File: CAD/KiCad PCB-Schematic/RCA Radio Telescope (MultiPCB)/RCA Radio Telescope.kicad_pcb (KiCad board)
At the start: 2 copper layers, 330.1 x 183.4 mm, 67 parts, among them J1 5V In For Filter Board, J10 FILTER_OUT, J11 ANT, J11 Screw_Terminal_01x04, J13 Screw_Terminal_01x04, J15 ANT, J2 9-12V From PoE Splitter, J3 3V Out For LNA, J4 5V Out For Filter Board, J5 Input from SDR, J7 USB_A, J8 USB_A, J9 ANT, Q1 DMP4047LFDE-7, U13 MAX8510EXK30T, U14 TPS62133RGTR, U15 BPF-A1340+, U3 SKY13588-460LF, U4 SKY13588-460LF, U5 SN74AVC2T45DCUR, U6 MIC5365-1.8YC5-TR, U7 MIC5365-3.3YC5-TR

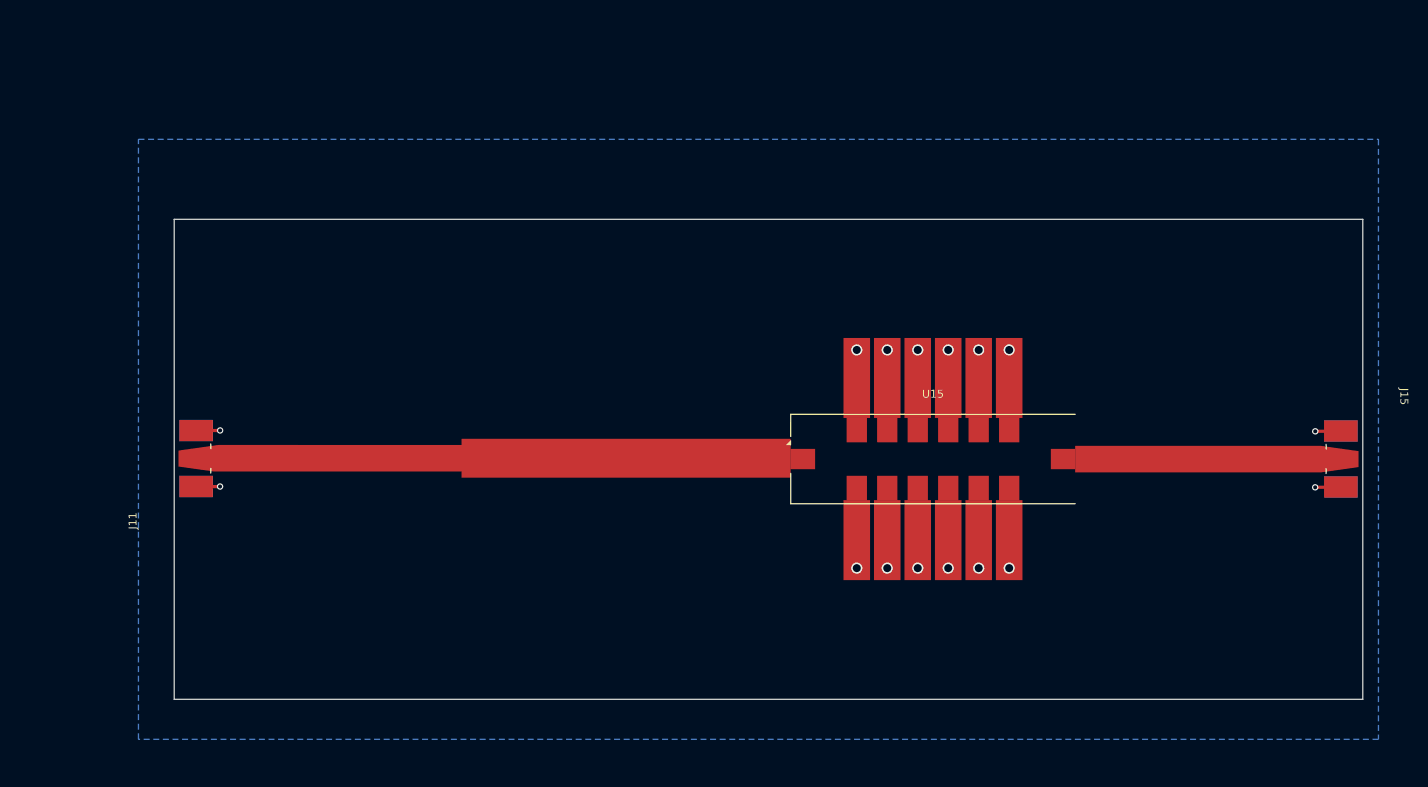
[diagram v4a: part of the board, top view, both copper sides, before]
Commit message: Updated SMD Filter PCB to v1.1
- Adjusted GND pads from 10 to 6mm
- Added M4 Holes for mounting
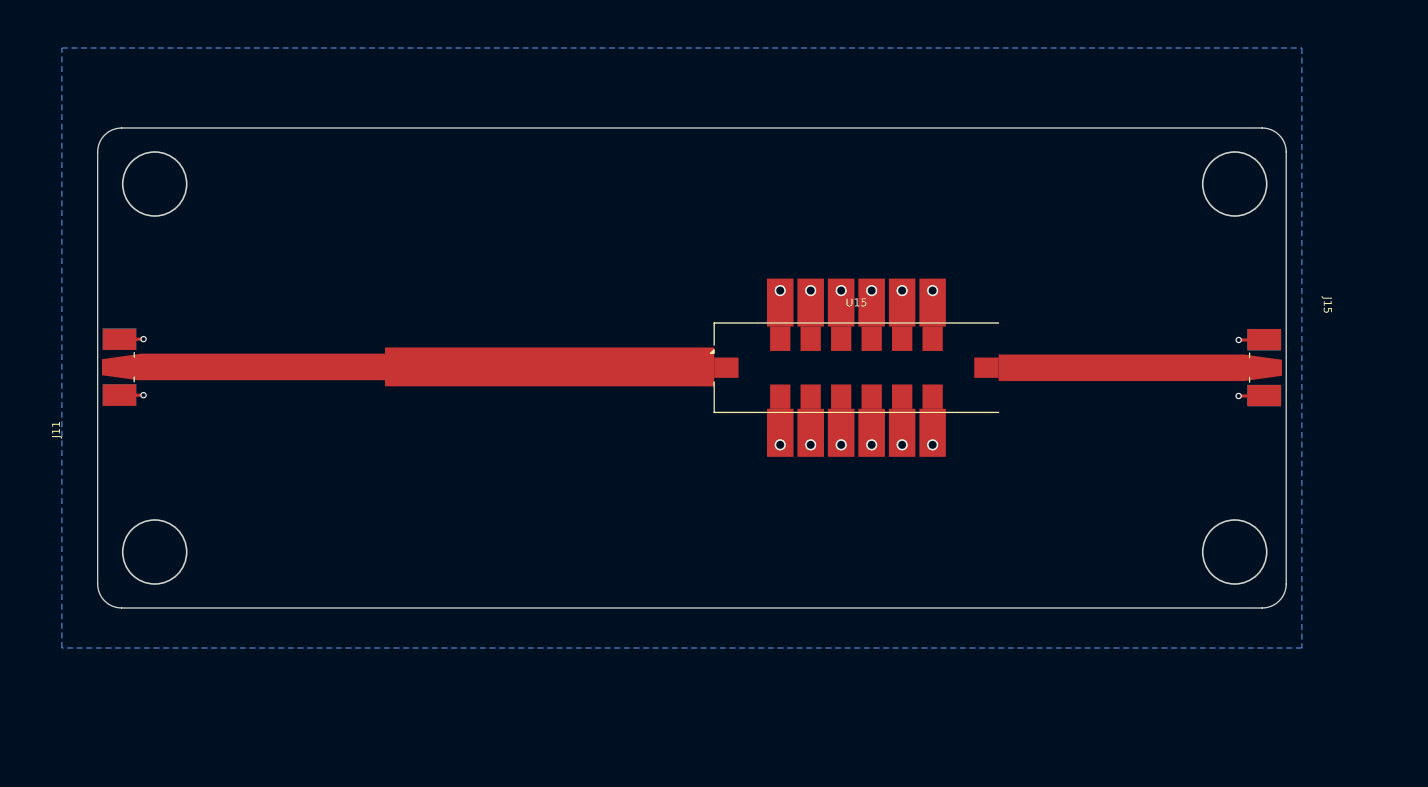
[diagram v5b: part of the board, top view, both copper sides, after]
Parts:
- moved J11 14.9 mm to (197.6, 89.9)
- moved U15 14.9 mm to (294.7, 90.0)
- moved J15 14.9 mm to (350.7, 90.0)
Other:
- board size 330.1 x 183.4 mm -> 320.5 x 183.4 mm
- board text added: "Pad Spacing: 3.81mm"
- board text added: "SMD Filter PCB Rev v1.1 4/9/2025"
- board text removed: "3.81mm"
- board text removed: "SMD Filter PCB Rev v1.0 4/8/2025"

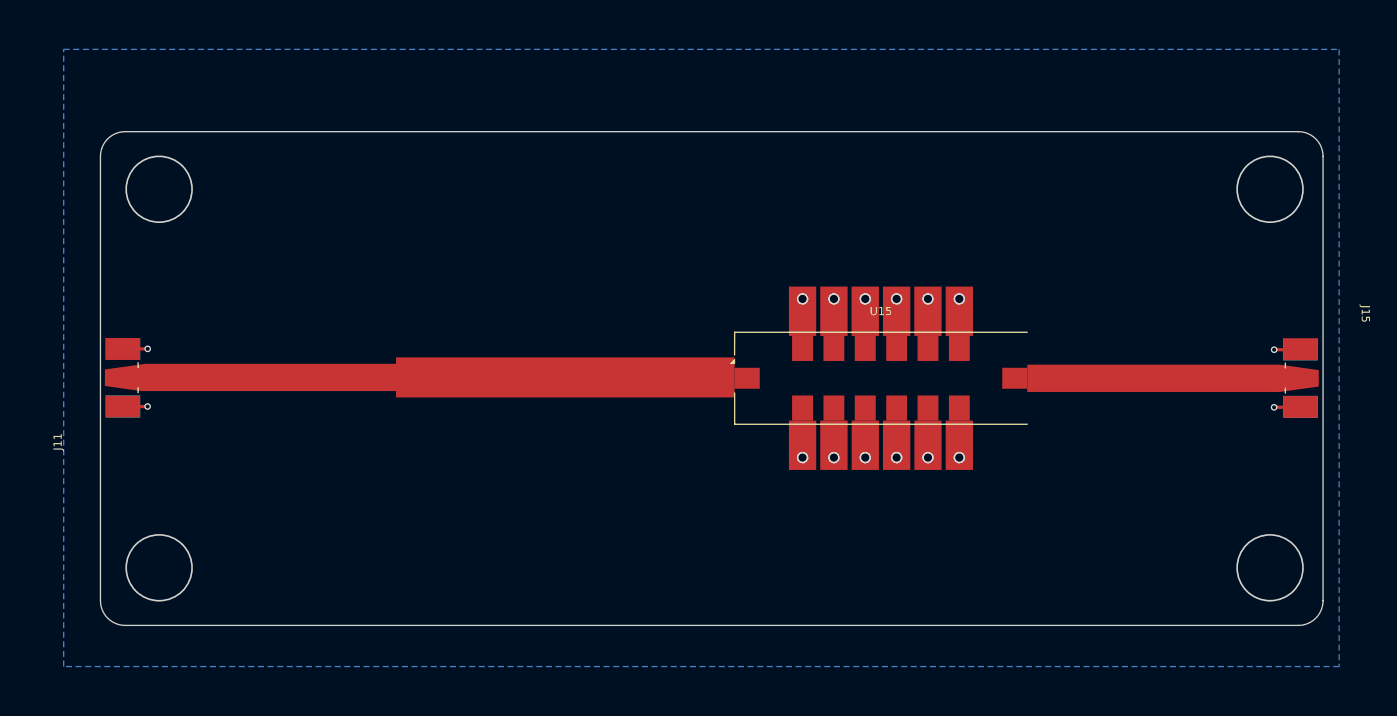
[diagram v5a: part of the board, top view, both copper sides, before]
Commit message: Updated SMD FIlter Board to v1.2
- Added KiKit Label
- Minor adjustments to PCB
- Exported to separate project

- Edited SMA connector footprint
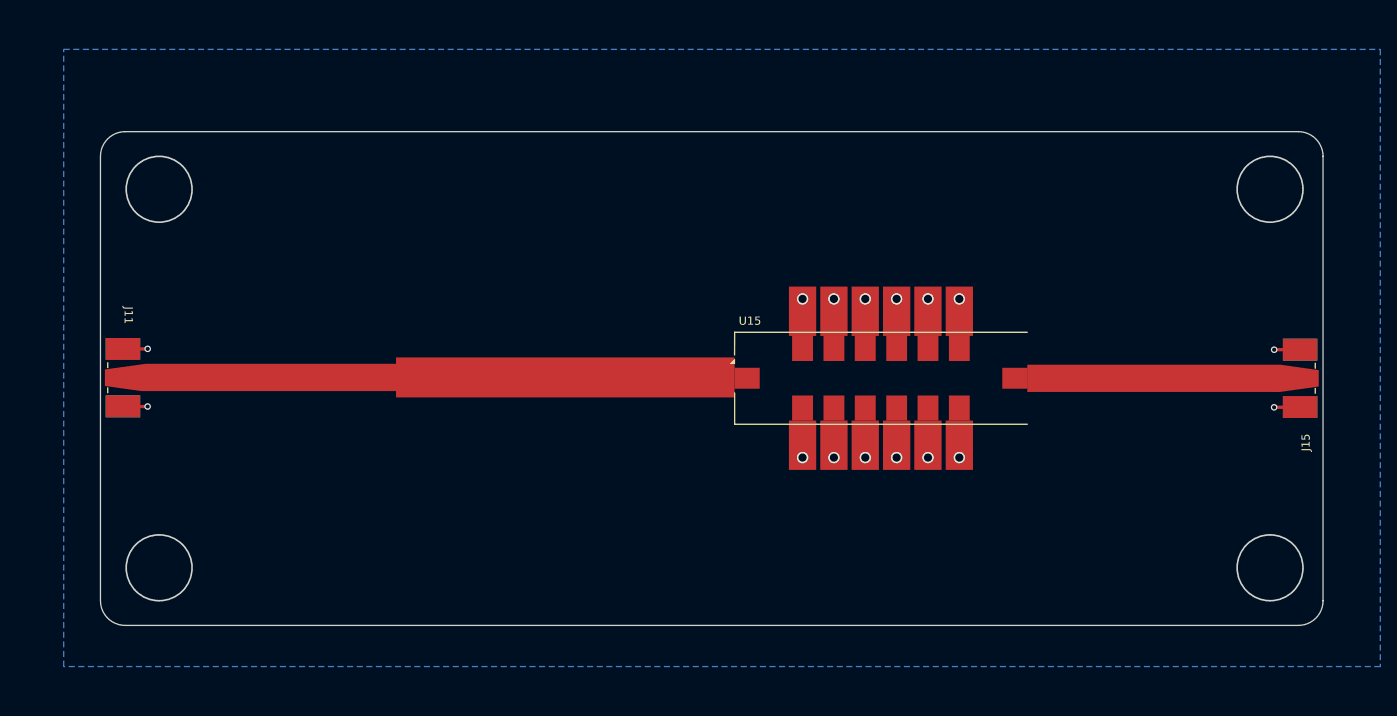
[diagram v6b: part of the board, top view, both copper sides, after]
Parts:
- added SF: Kikit_Board_Label, Library:Kikit_Board_Label, F.Cu at (215.8, 60.0)
- moved J15 9.96 mm to (340.7, 90.0), turned to 90 degrees
- moved J11 9.91 mm to (207.6, 89.9), turned to -90 degrees
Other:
- board text added: "SMD Filter PCB Rev v1.2 4/9/2025"
- board text removed: "SMD Filter PCB Rev v1.1 4/9/2025"

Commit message: Add Measurement Text for Boards
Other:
- board text added: "Length: 135 mm Width: 46 mm Hole Diameter: 8 mm"
- board text added: "Length: 48 mm Width: 28 mm Hole Diameter: 6 mm"
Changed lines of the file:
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@@
+		)
+	)
+	(gr_text "Length: 135 mm\nWidth: 46 mm\nHole Diameter: 8 mm"
+		(at 261 147 0)
+		(layer "User.3")
+		(effects
+			(font
+				(size 4 4)
+				(thickness 1)
+				(bold yes)
+			)
+			(justify left bottom)
+		)
+	)
+	(gr_text "Length: 48 mm\nWidth: 28 mm\nHole Diameter: 6 mm"
+		(at 69 85 0)
+		(layer "User.3")
+		(effects
+			(font
+				(size 2 2)
+				(thickness 0.375)
+				(bold yes)
+			)
+			(justify left bottom)
 		)
 	)

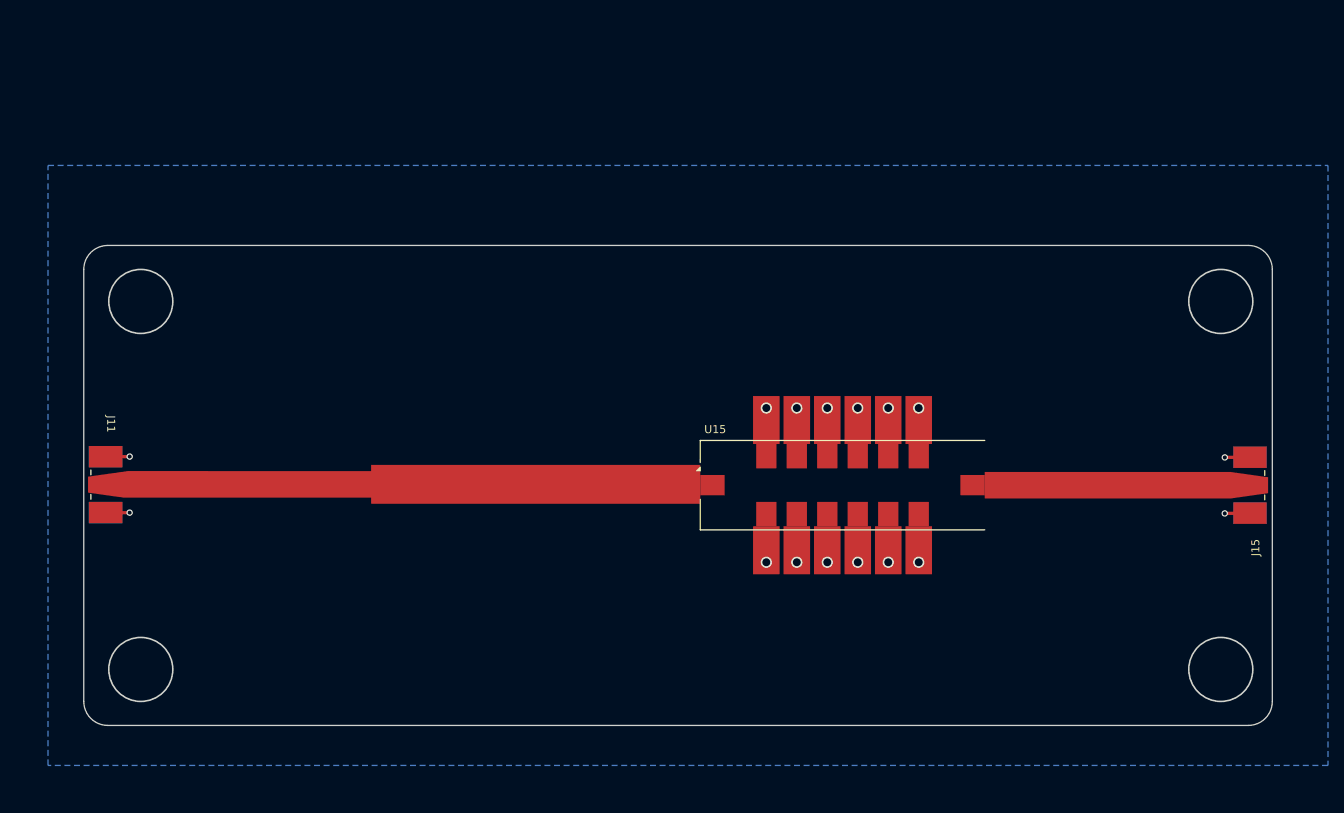
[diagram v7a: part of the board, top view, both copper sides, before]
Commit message: Updated SMD FIlter Board to v1.3
- Adjusted line length to remove 39 ohm segment
- Updated screwholes to be correct size
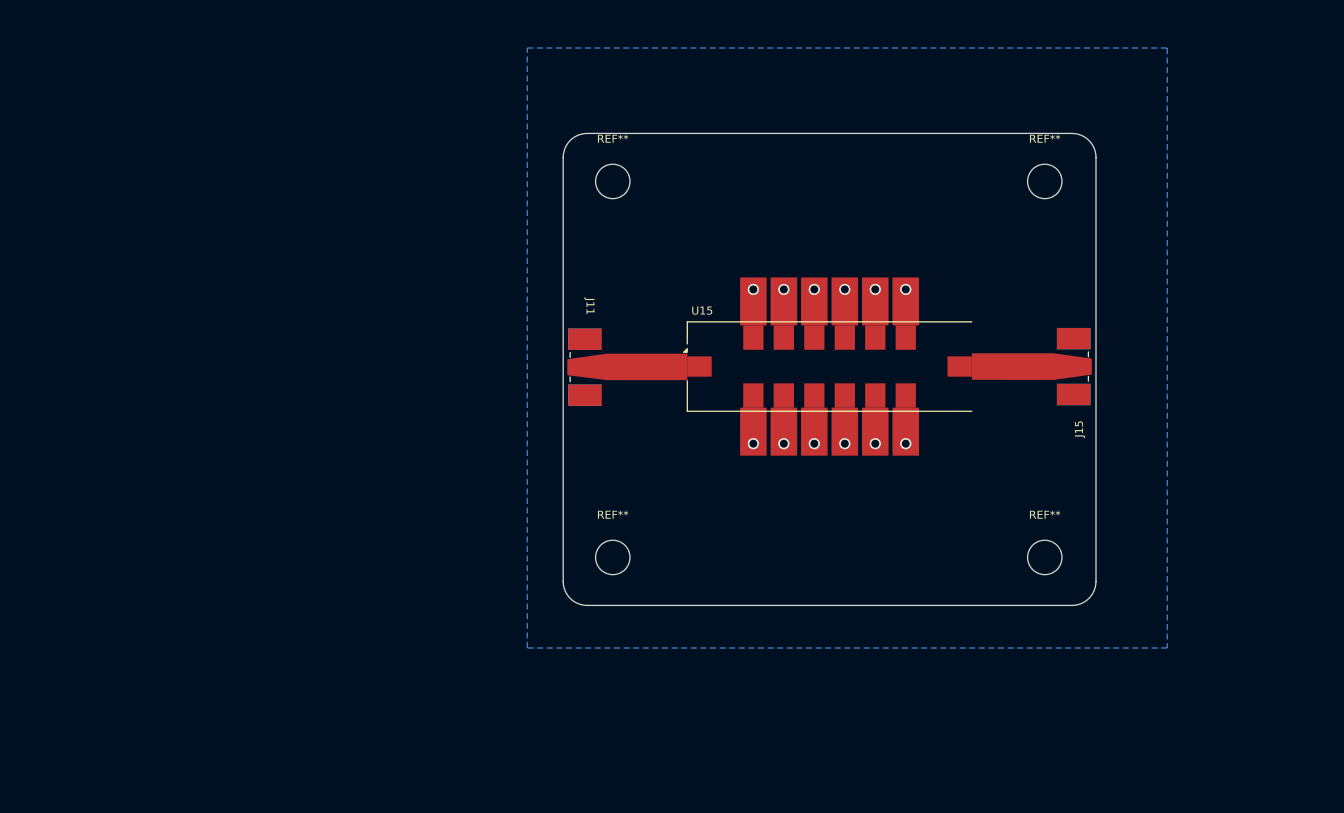
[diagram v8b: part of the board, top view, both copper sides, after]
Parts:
- added REF**: MountingHole_4.3mm_M4, MountingHole:MountingHole_4.3mm_M4, F.Cu at (320.0, 99.0)
- added REF**: MountingHole_4.3mm_M4, MountingHole:MountingHole_4.3mm_M4, F.Cu at (266.0, 52.0)
- added REF**: MountingHole_4.3mm_M4, MountingHole:MountingHole_4.3mm_M4, F.Cu at (266.0, 99.0)
- added REF**: MountingHole_4.3mm_M4, MountingHole:MountingHole_4.3mm_M4, F.Cu at (320.0, 52.0)
- moved SF 61.8 mm to (276.0, 46.0)
- moved J11 61.7 mm to (267.5, 75.2)
- moved J15 26.6 mm to (318.7, 75.1)
- moved U15 14.9 mm to (293.1, 75.1)
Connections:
- J11 pad 3: /SMDFilter/GND -> (no net)
- J11 pad 5: /SMDFilter/GND -> (no net)
- J15 pad 3: /SMDFilter/GND -> (no net)
- J15 pad 5: /SMDFilter/GND -> (no net)
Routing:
- net /SMDFilter/GND: track 11.6 -> 0.00 mm, vias 16 -> 12
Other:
- board size 320.5 x 183.4 mm -> 298.5 x 183.4 mm
- board text added: "Length: 54 mm Width: 47 mm Hole Diameter: 4 mm"
- board text added: "SMD Filter PCB Rev v1.3 4/11/2025"
- board text removed: "Length: 135 mm Width: 46 mm Hole Diameter: 8 mm"
- board text removed: "SMD Filter PCB Rev v1.2 4/9/2025"
